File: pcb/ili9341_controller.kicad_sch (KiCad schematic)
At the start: 56 parts, among them J1 USB_B_Micro, J2 RP_SWD_CONN, SW1 RP_RST_SW, SW2 RP_USB_BOOT_SW, U1 ICE40UP5K-SG48ITR, U2 LM3880, U3 LD1117S33TR_SOT223, U4 LD1117S12TR_SOT223, U5 LD1117S25TR_SOT223, U6 RP2040, U7 W25Q128JVS, Y1 12MHz

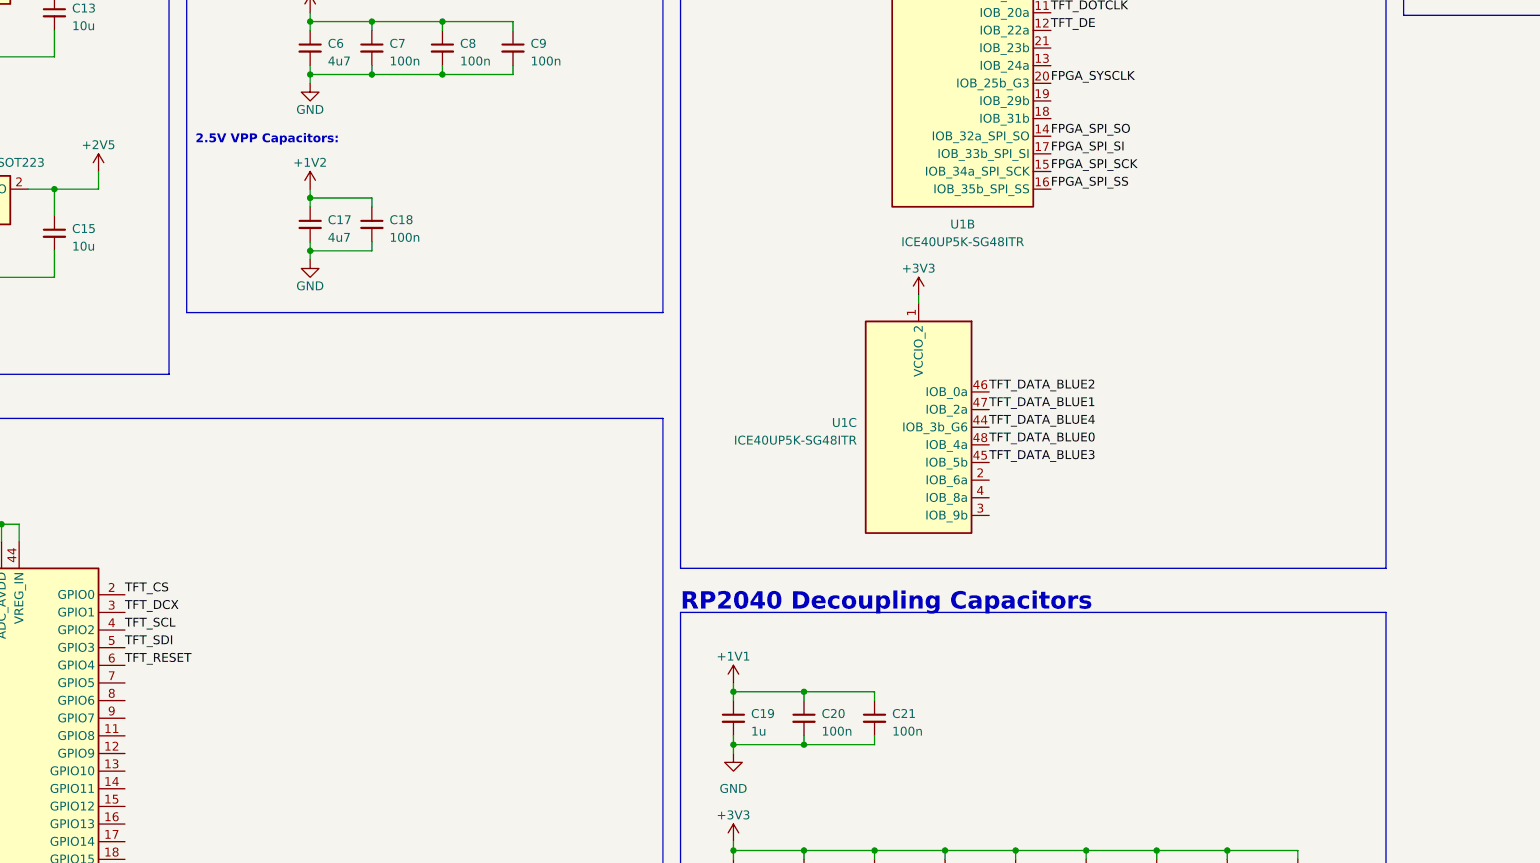
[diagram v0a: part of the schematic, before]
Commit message: add configuration connections for fpga to rp2040
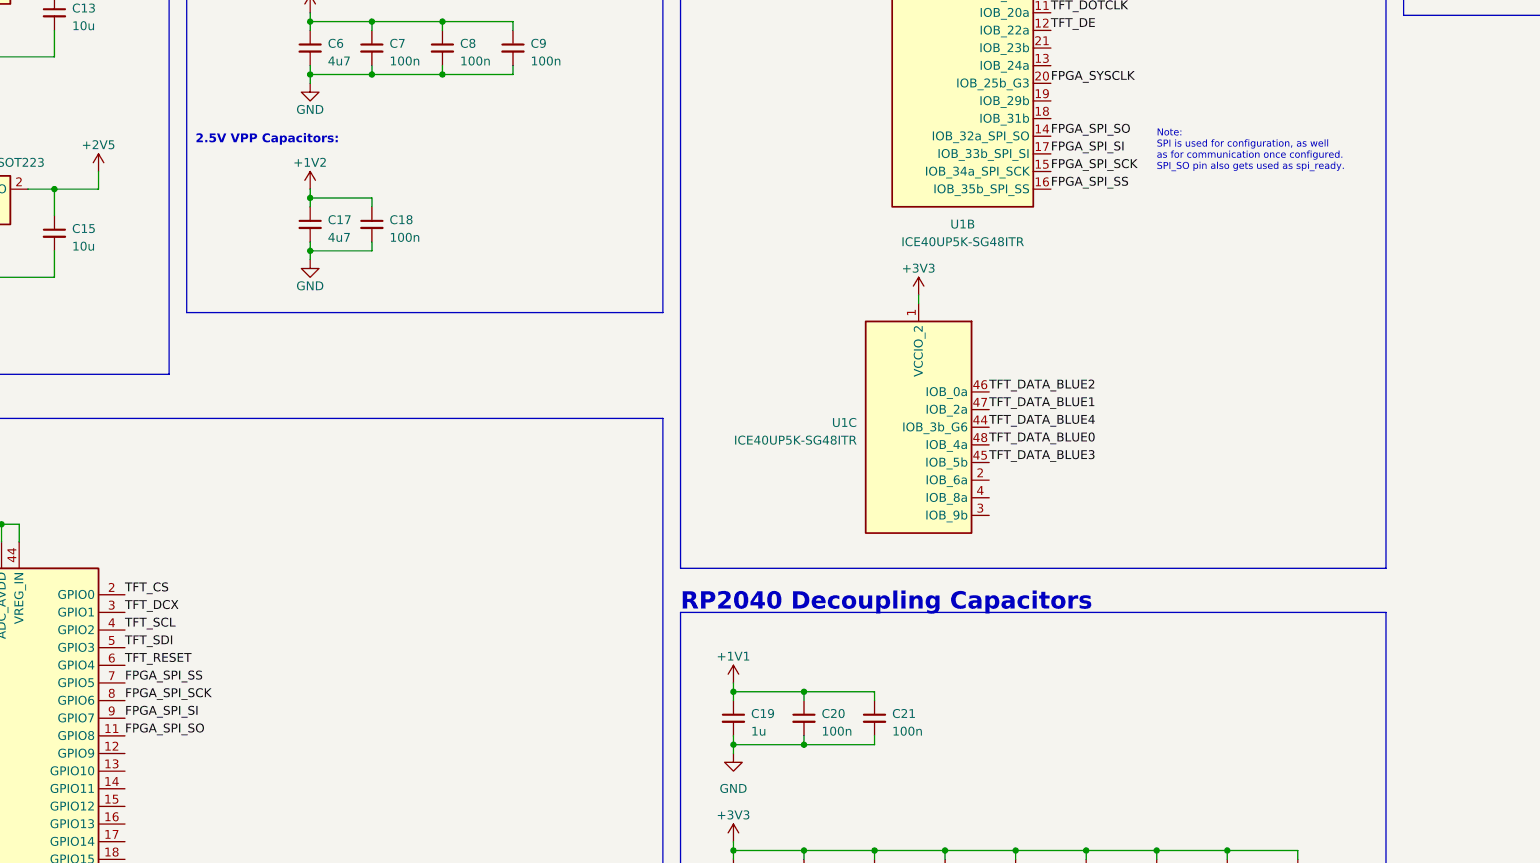
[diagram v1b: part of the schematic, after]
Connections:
- net FPGA_SPI_SCK: now also U6.8 (GPIO6)
- net FPGA_SPI_SI: now also U6.9 (GPIO7)
- net FPGA_SPI_SO: now also U6.11 (GPIO8)
- net FPGA_SPI_SS: now also U6.7 (GPIO5)
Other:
- note added: "Note: SPI is used for configuration, as well as for communication once configured. SPI_SO pin also gets used as spi_ready."
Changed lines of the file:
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@@
     (effects (font (size 2.5 2.5) (thickness 0.5) bold) (justify left bottom))
+  )
+  (text "Note:\nSPI is used for configuration, as well\nas for communication once configured.\nSPI_SO pin also gets used as spi_ready."
+    (at 287.02 161.29 0)
+    (effects (font (size 1 1)) (justify left bottom))
   )
   (text "USB Connector" (at 25.4 25.4 0)
@@
     (effects (font (size 0.75 0.75)) (justify left bottom))
   )
+  (label "FPGA_SPI_SO" (at 138.43 242.57 0) (fields_autoplaced)
+    (effects (font (size 1.27 1.27)) (justify left bottom))
+  )
   (label "TFT_DATA_BLUE4" (at 405.13 93.98 0) (fields_autoplaced)
     (effects (font (size 1.27 1.27)) (justify left bottom))
@@
     (effects (font (size 0.75 0.75)) (justify right bottom))
   )
+  (label "FPGA_SPI_SCK" (at 138.43 237.49 0) (fields_autoplaced)
+    (effects (font (size 1.27 1.27)) (justify left bottom))
+  )
   (label "TFT_DATA_GREEN5" (at 262.89 73.66 0) (fields_autoplaced)
     (effects (font (size 1.27 1.27)) (justify left bottom))
@@
     (effects (font (size 1.27 1.27)) (justify left bottom))
   )
+  (label "FPGA_SPI_SS" (at 138.43 234.95 0) (fields_autoplaced)
+    (effects (font (size 1.27 1.27)) (justify left bottom))
+  )
   (label "TFT_DATA_RED1" (at 405.13 71.12 0) (fields_autoplaced)
     (effects (font (size 1.27 1.27)) (justify left bottom))
   )
+  (label "FPGA_SPI_SI" (at 138.43 240.03 0) (fields_autoplaced)
+    (effects (font (size 1.27 1.27)) (justify left bottom))
+  )

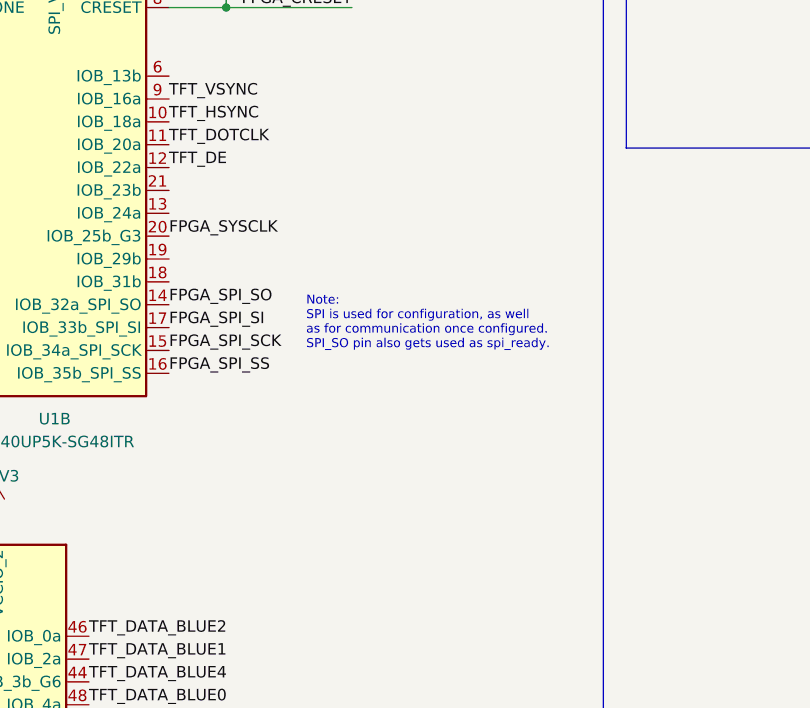
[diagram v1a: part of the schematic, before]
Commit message: add pull up and pull downs for configuration pins
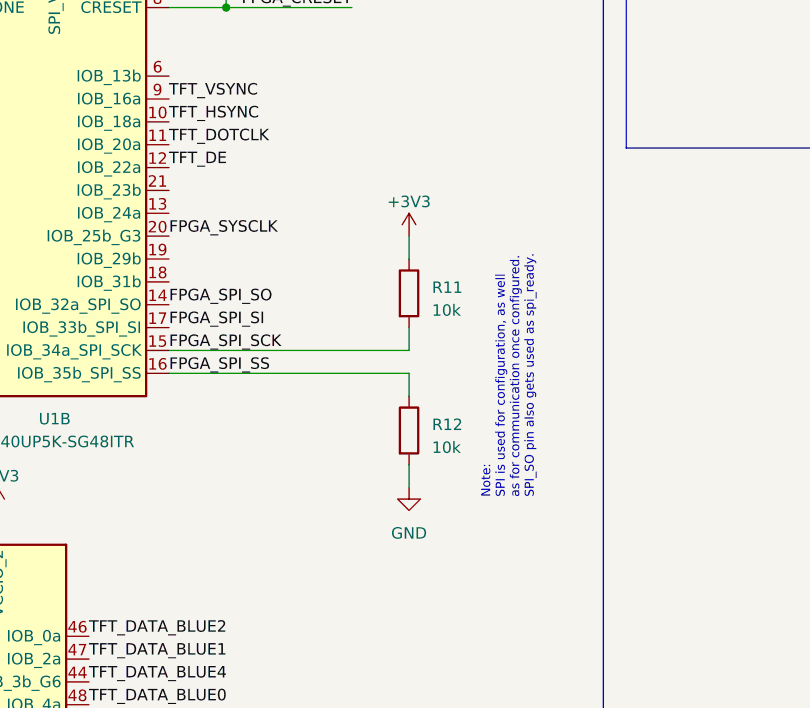
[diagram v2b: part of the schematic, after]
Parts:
- added R11, R12: 10k, symbol Device:R
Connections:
- net +3V3: now also R11.1
- net FPGA_SPI_SCK: now also R11.2
- net FPGA_SPI_SS: now also R12.1
- net GND: now also R12.2
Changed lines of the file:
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@@
+    (stroke (width 0) (type default))
+  )
+  (wire (pts (xy 298.45 176.53) (xy 298.45 173.99))
     (stroke (width 0) (type default))
   )
@@
     (stroke (width 0) (type default))
   )
+  (wire (pts (xy 298.45 148.59) (xy 298.45 151.13))
+    (stroke (width 0) (type default))
+  )
   (wire (pts (xy 236.22 236.22) (xy 246.38 236.22))
     (stroke (width 0) (type default))
@@
     (stroke (width 0) (type default))
   )
+  (wire (pts (xy 298.45 158.75) (xy 298.45 161.29))
+    (stroke (width 0) (type default))
+  )
   (wire (pts (xy 128.27 163.83) (xy 134.62 163.83))
     (stroke (width 0) (type default))
@@
     (stroke (width 0) (type default))
   )
+  (wire (pts (xy 271.78 161.29) (xy 298.45 161.29))
+    (stroke (width 0) (type default))
+  )
   (wire (pts (xy 104.14 100.33) (xy 109.22 100.33))
     (stroke (width 0) (type default))
@@
     (stroke (width 0) (type default))
   )
+  (wire (pts (xy 298.45 163.83) (xy 298.45 166.37))
+    (stroke (width 0) (type default))
+  )
   (wire (pts (xy 184.15 97.79) (xy 184.15 99.06))
     (stroke (width 0) (type default))
@@
   )
   (wire (pts (xy 46.99 49.53) (xy 60.96 49.53))
+    (stroke (width 0) (type default))
+  )
+  (wire (pts (xy 271.78 163.83) (xy 298.45 163.83))
     (stroke (width 0) (type default))
   )
@@
   )
   (text "Note:\nSPI is used for configuration, as well\nas for communication once configured.\nSPI_SO pin also gets used as spi_ready."
-    (at 287.02 161.29 0)
+    (at 312.42 177.8 90)
     (effects (font (size 1 1)) (justify left bottom))
   )
@@
         (path "/5ab5cbe5-2e2b-40a8-992c-b266cf7668f6"
           (reference "C11") (unit 1)
+        )
+      )
+    )
+  )
+  (symbol (lib_id "power:+3V3") (at 298.45 148.59 0) (unit 1)
+    (in_bom yes) (on_board yes) (dnp no) (fields_autoplaced)
+    (property "Reference" "#PWR047" (at 298.45 152.4 0)
+      (effects (font (size 1.27 1.27)) hide)
+    )
+    (property "Value" "+3V3" (at 298.45 144.78 0)
+      (effects (font (size 1.27 1.27)))
+    )
+    (property "Footprint" "" (at 298.45 148.59 0)
+      (effects (font (size 1.27 1.27)) hide)
+    )
+    (property "Datasheet" "" (at 298.45 148.59 0)
+      (effects (font (size 1.27 1.27)) hide)
+    )
+    (pin "1")
+    (instances
+      (project "ili9341_controller"
+        (path "/5ab5cbe5-2e2b-40a8-992c-b266cf7668f6"
+          (reference "#PWR047") (unit 1)
         )
       )
@@
     )
   )
+  (symbol (lib_id "power:GND") (at 298.45 176.53 0) (unit 1)
+    (in_bom yes) (on_board yes) (dnp no) (fields_autoplaced)
+    (property "Reference" "#PWR048" (at 298.45 182.88 0)
+      (effects (font (size 1.27 1.27)) hide)
+    )
+    (property "Value" "GND" (at 298.45 181.61 0)
+      (effects (font (size 1.27 1.27)))
+    )
+    (property "Footprint" "" (at 298.45 176.53 0)
+      (effects (font (size 1.27 1.27)) hide)
+    )
+    (property "Datasheet" "" (at 298.45 176.53 0)
+      (effects (font (size 1.27 1.27)) hide)
+    )
+    (pin "1")
+    (instances
+      (project "ili9341_controller"
+        (path "/5ab5cbe5-2e2b-40a8-992c-b266cf7668f6"
+          (reference "#PWR048") (unit 1)
+        )
+      )
+    )
+  )
   (symbol (lib_id "Device:C_Small") (at 246.38 262.89 0) (unit 1)
     (in_bom yes) (on_board yes) (dnp no) (fields_autoplaced)
@@
         (path "/5ab5cbe5-2e2b-40a8-992c-b266cf7668f6"
           (reference "C13") (unit 1)
+        )
+      )
+    )
+  )
+  (symbol (lib_id "Device:R") (at 298.45 170.18 0) (unit 1)
+    (in_bom yes) (on_board yes) (dnp no) (fields_autoplaced)
+    (property "Reference" "R12" (at 300.99 169.545 0)
+      (effects (font (size 1.27 1.27)) (justify left))
+    )
+    (property "Value" "10k" (at 300.99 172.085 0)
+      (effects (font (size 1.27 1.27)) (justify left))
+    )
+    (property "Footprint" "" (at 296.672 170.18 90)
+      (effects (font (size 1.27 1.27)) hide)
+    )
+    (property "Datasheet" "~" (at 298.45 170.18 0)
+      (effects (font (size 1.27 1.27)) hide)
+    )
+    (pin "1")
+    (pin "2")
+    (instances
+      (project "ili9341_controller"
+        (path "/5ab5cbe5-2e2b-40a8-992c-b266cf7668f6"
+          (reference "R12") (unit 1)
         )
       )
@@
         )
       )
+    )
+  )
+  (symbol (lib_id "Device:R") (at 298.45 154.94 0) (unit 1)
+    (in_bom yes) (on_board yes) (dnp no) (fields_autoplaced)
+    (property "Reference" "R11" (at 300.99 154.305 0)
+      (effects (font (size 1.27 1.27)) (justify left))
+    )
+    (property "Value" "10k" (at 300.99 156.845 0)
+      (effects (font (size 1.27 1.27)) (justify left))
+    )
+    (property "Footprint" "" (at 296.672 154.94 90)
+      (effects (font (size 1.27 1.27)) hide)
+    )
+    (property "Datasheet" "~" (at 298.45 154.94 0)
+      (effects (font (size 1.27 1.27)) hide)
+    )
+    (pin "1")
+    (pin "2")
+    (instances
+      (project "ili9341_controller"
+        (path "/5ab5cbe5-2e2b-40a8-992c-b266cf7668f6"
+          (reference "R11") (unit 1)
+        )
+      )
